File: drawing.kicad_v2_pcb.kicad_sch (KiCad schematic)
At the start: 39 parts, among them IC1 DW01A-G, J1 Micro USB Chargeport, J2 Prog headers, J3 128x32 I2C OLED, J4 TP4056, J5 MK-12C02, J6 Conn_01x02, Q1 FS8205, U1 HT7333-SOT89, U2 ESP-12E, U3 ATTINY85-20PU

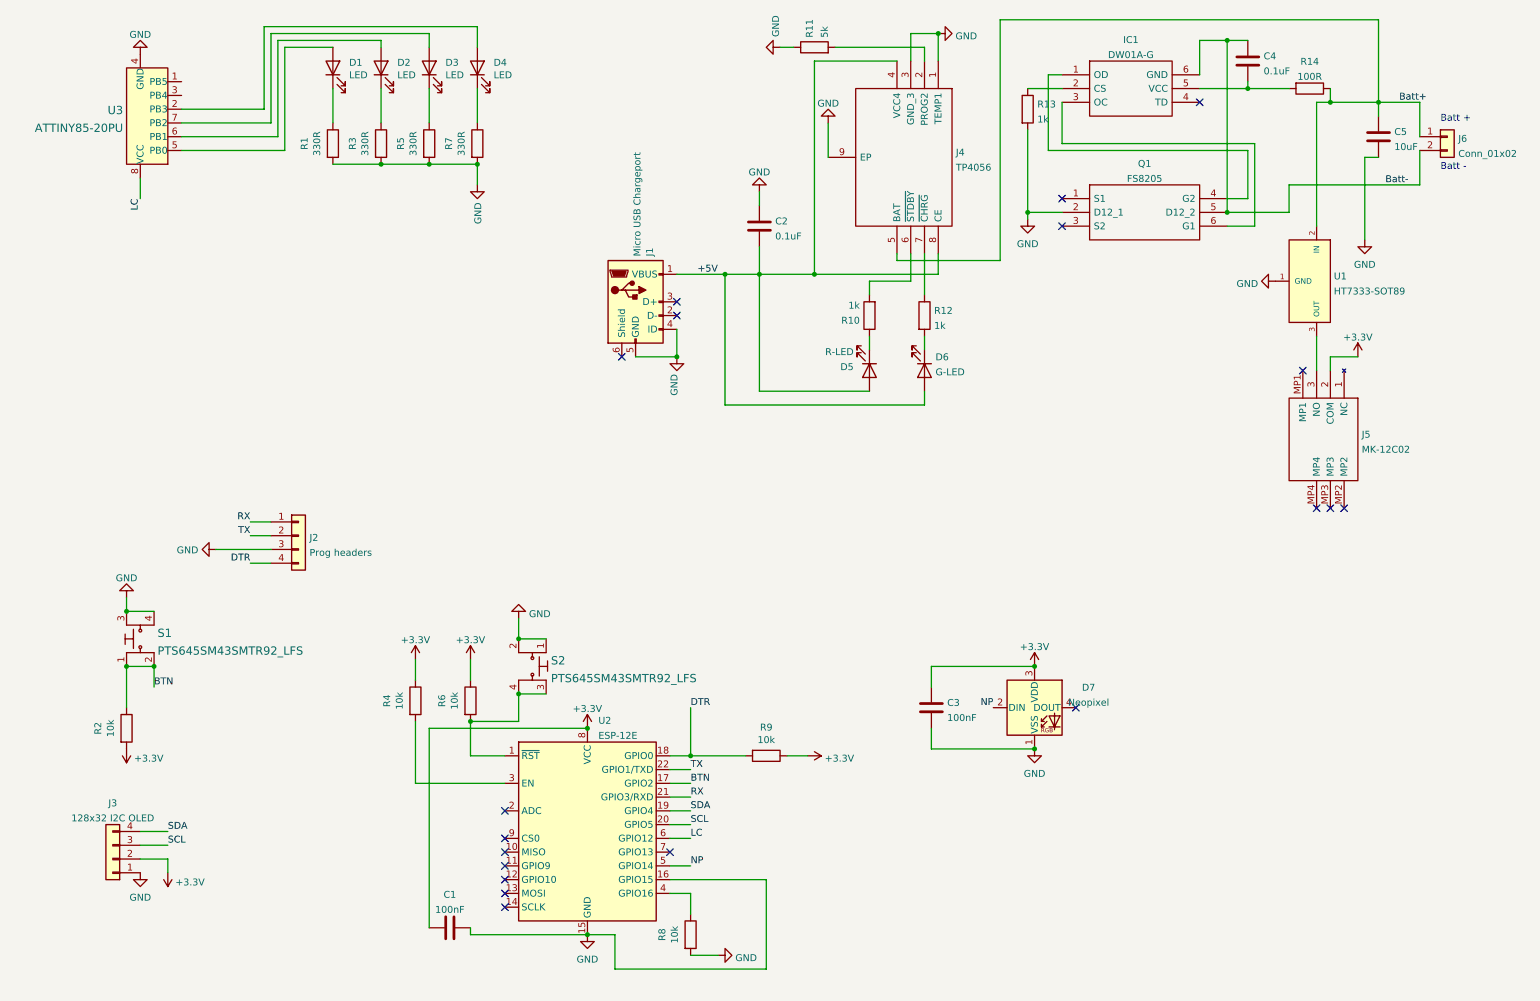
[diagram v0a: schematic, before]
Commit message: Fixed HT7333 and charging circuit
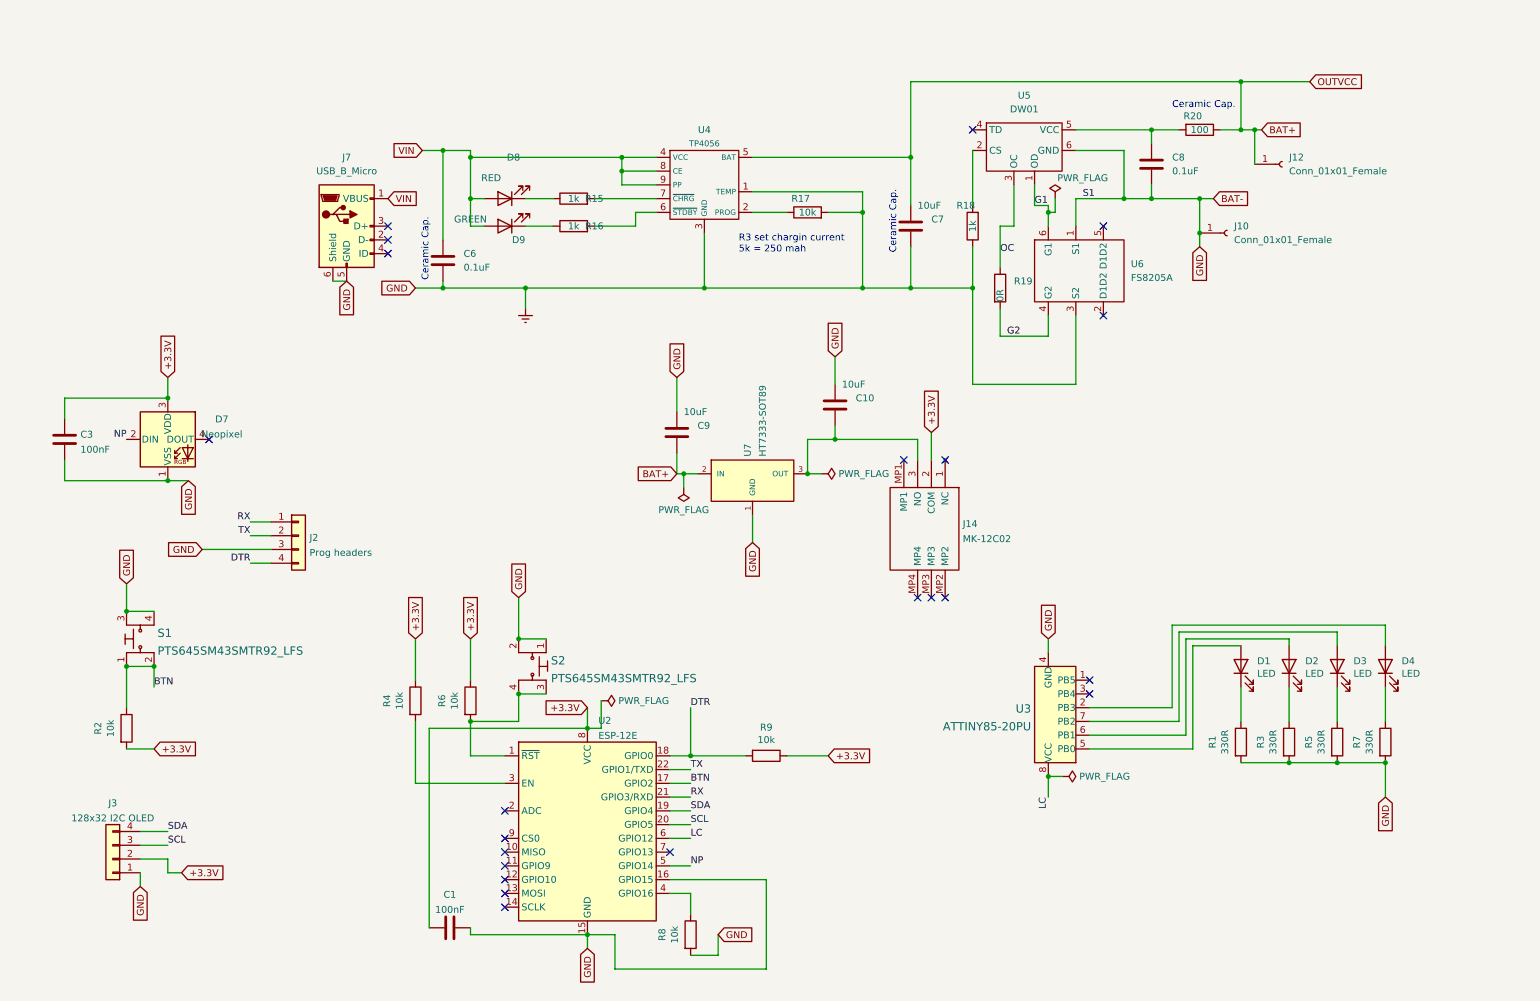
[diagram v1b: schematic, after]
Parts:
- removed C2, C4: 0.1uF, Capacitor_SMD:C_0805_2012Metric_Pad1.18x1.45mm_HandSolder, symbol Device:C
- removed C5: 10uF, Capacitor_SMD:C_0805_2012Metric_Pad1.18x1.45mm_HandSolder, symbol Device:C
- removed D5: R-LED, LED_SMD:LED_0805_2012Metric_Pad1.15x1.40mm_HandSolder, symbol Device:LED
- removed D6: G-LED, LED_SMD:LED_0805_2012Metric_Pad1.15x1.40mm_HandSolder, symbol Device:LED
- removed IC1: DW01A-G, user-footprints:SOT95P280X135-6N, symbol DW01A-G:DW01A-G
- removed J1: Micro USB Chargeport, digikey-footprints:USB_Micro_B_Female_10118194-0001LF, symbol Connector:USB_B_Micro
- removed J4: TP4056, Custom:SOIC127P600X175-9N, symbol TP4056:TP4056
- removed J5: MK-12C02, user-footprints:MK12C02, symbol MK-12C02:MK-12C02
- removed J6: Conn_01x02, Connector_JST:JST_EH_B2B-EH-A_1x02_P2.50mm_Vertical, symbol Connector_Generic:Conn_01x02
- removed Q1: FS8205, user-footprints:FS8205, symbol FS8205:FS8205
- removed R10, R12, R13: 1k, Resistor_SMD:R_0805_2012Metric_Pad1.20x1.40mm_HandSolder, symbol Device:R
- removed R11: 5k, Resistor_SMD:R_0805_2012Metric_Pad1.20x1.40mm_HandSolder, symbol Device:R
- removed R14: 100R, Resistor_SMD:R_0805_2012Metric_Pad1.20x1.40mm_HandSolder, symbol Device:R
- removed U1: HT7333-SOT89, Custom:Holtek-HT7333-SOT89-Level_A, symbol eec:HT7333-SOT89
- added C10, C7, C9: 10uF, Capacitor_SMD:C_0805_2012Metric_Pad1.18x1.45mm_HandSolder, symbol Device:C
- added C6, C8: 0.1uF, Capacitor_SMD:C_0805_2012Metric_Pad1.18x1.45mm_HandSolder, symbol Device:C
- added D8: RED, LED_SMD:LED_0805_2012Metric_Pad1.15x1.40mm_HandSolder, symbol Device:LED
- added D9: GREEN, LED_SMD:LED_0805_2012Metric_Pad1.15x1.40mm_HandSolder, symbol Device:LED
- added J10, J12: Conn_01x01_Female, user-footprints:solderpad, symbol Connector:Conn_01x01_Female
- added J14: MK-12C02, user-footprints:MK12C02, symbol MK-12C02:MK-12C02
- added J7: USB_B_Micro, digikey-footprints:USB_Micro_B_Female_10118194-0001LF, symbol Connector:USB_B_Micro
- added R15, R16, R18: 1k, Resistor_SMD:R_0603_1608Metric_Pad0.98x0.95mm_HandSolder, symbol Device:R
- added R17: 10k, Resistor_SMD:R_0805_2012Metric_Pad1.20x1.40mm_HandSolder, symbol Device:R
- added R19: 0R, Resistor_SMD:R_1206_3216Metric_Pad1.30x1.75mm_HandSolder, symbol Device:R
- added R20: 100, Resistor_SMD:R_0805_2012Metric_Pad1.20x1.40mm_HandSolder, symbol Device:R
- added U4: TP4056, Package_SO:SOIC-8-1EP_3.9x4.9mm_P1.27mm_EP2.29x3mm, symbol tp4056:TP4056
- added U5: DW01, Package_TO_SOT_SMD:SOT-23-6_Handsoldering, symbol dw01:DW01
- added U6: FS8205A, Package_TO_SOT_SMD:SOT-23-6_Handsoldering, symbol fs8205:FS8205A
- added U7: HT7333-SOT89, user-footprints:Holtek-HT7333-SOT89-Level_A, symbol eec:HT7333-SOT89
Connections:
- net +3V3 renamed +3.3V
- net +3.3V: now also J14.2 (COM)
- net GND renamed Earth
- net Earth: now also C10.1, C6.2, C7.2, C8.2, C9.1, J10.1 (Pin_1), J7.5 (GND), J7.6 (Shield), R17.2, R18.1, U4.1 (TEMP), U4.3 (GND), U5.6 (GND), U6.1 (S1), U6.3 (S2), U7.1 (GND)
- new net: C10.2, J14.3 (NO), U7.3 (OUT)
- new net: R18.2, U5.2 (CS)
- new net: D9.1 (K), R16.1
- new net: R17.1, U4.2 (PROG)
- new net: R16.2, U4.6 (~{STDBY})
- new net: R15.2, U4.7 (~{CHRG})
- new net: C8.1, R20.2, U5.5 (VCC)
- new net: D8.1 (K), R15.1
- new net BAT+: C7.1, C9.2, J12.1 (Pin_1), R20.1, U4.5 (BAT), U7.2 (IN)
- new net G1: U5.1 (OD), U6.6 (G1)
- new net G2: R19.2, U6.4 (G2)
- new net OC: R19.1, U5.3 (OC)
- new net VIN: C6.1, D8.2 (A), D9.2 (A), J7.1 (VBUS), U4.4 (VCC), U4.8 (CE), U4.9 (PP)
- no-connect marks 19 -> 22
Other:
- note added: "Ceramic Cap."
- note added: "R3 set chargin current 5k = 250 mah"
- note removed: "Batt +"
- note removed: "Batt -"
- moved on the sheet: C3, D1, D2, D3, D4, D7, R1, R3, R5, R7, U3

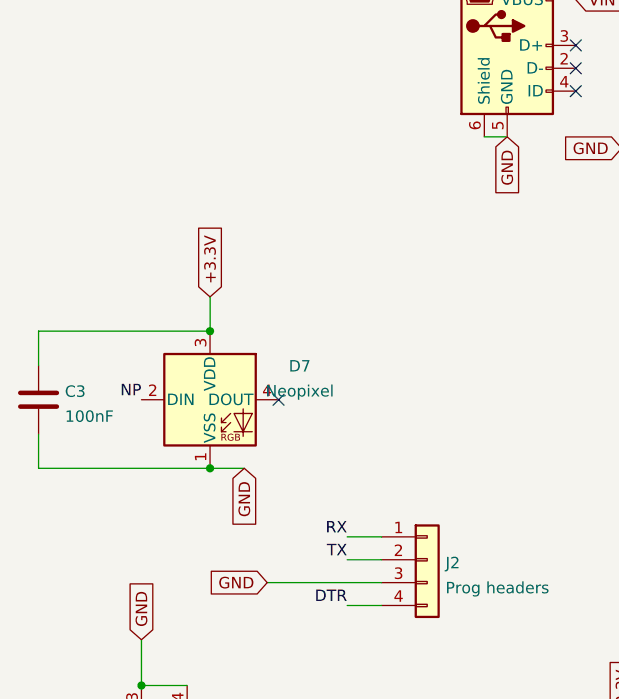
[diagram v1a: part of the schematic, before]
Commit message: Changed TH components to SMD
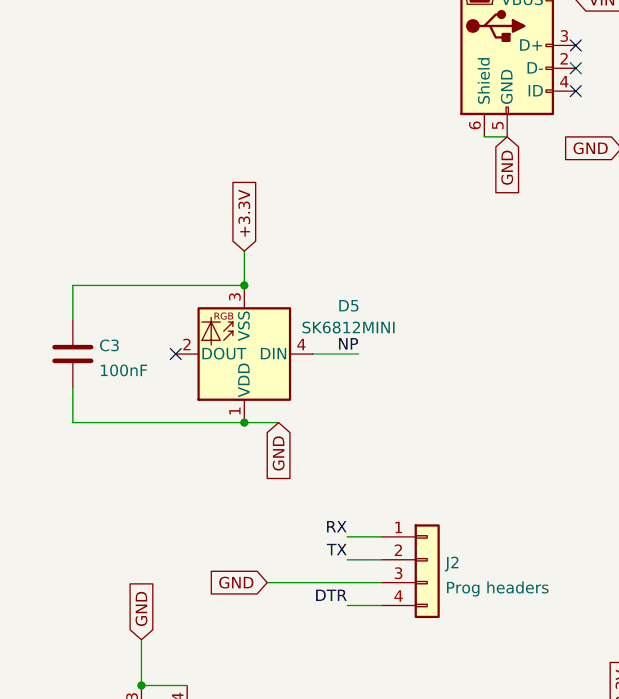
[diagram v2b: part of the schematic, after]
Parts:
- removed D7: Neopixel, user-footprints:LED_SK6812_PLCC4_5.0x5.0mm_P3.2mm_mirror, symbol LED:SK6812
- added D5: SK6812MINI, LED_SMD:LED_SK6812MINI_PLCC4_3.5x3.5mm_P1.75mm, symbol sk6812mini-e:SK6812MINI-E
- U3: footprint digikey-footprints:DIP-8_W7.62mm -> Package_DIP:SMDIP-8_W7.62mm
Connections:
- net +3.3V: now also D5.3 (VSS)
- net Earth: now also D5.1 (VDD)
- net NP: now also D5.4 (DIN)
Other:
- moved on the sheet: C3
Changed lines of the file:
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@@
   (junction (at 139.7 63.5) (diameter 0) (color 0 0 0 0)
   )
+  (junction (at 44.45 93.98) (diameter 0) (color 0 0 0 0)
+  )
   (junction (at 106.68 63.5) (diameter 0) (color 0 0 0 0)
   )
@@
   (junction (at 105.41 138.43) (diameter 0) (color 0 0 0 0)
   )
-  (junction (at 40.64 99.06) (diameter 0) (color 0 0 0 0)
+  (junction (at 44.45 78.74) (diameter 0) (color 0 0 0 0)
   )
   (junction (at 177.8 39.37) (diameter 0) (color 0 0 0 0)
@@
   )
   (junction (at 247.65 151.13) (diameter 0) (color 0 0 0 0)
-  )
-  (junction (at 40.64 83.82) (diameter 0) (color 0 0 0 0)
   )
   (junction (at 168.91 49.53) (diameter 0) (color 0 0 0 0)
@@
   (no_connect (at 213.36 52.07))
   (no_connect (at 184.15 95.25))
+  (no_connect (at 36.83 86.36))
   (no_connect (at 81.28 54.61))
   (no_connect (at 179.07 120.65))
@@
   (no_connect (at 102.87 172.72))
   (no_connect (at 102.87 175.26))
-  (no_connect (at 48.26 91.44))
   (no_connect (at 176.53 95.25))
   (no_connect (at 210.82 138.43))
@@
     (stroke (width 0) (type default))
   )
-  (wire (pts (xy 21.59 83.82) (xy 40.64 83.82))
+  (wire (pts (xy 25.4 78.74) (xy 44.45 78.74))
     (stroke (width 0) (type default))
   )
@@
     (stroke (width 0) (type default))
   )
-  (wire (pts (xy 21.59 87.63) (xy 21.59 83.82))
+  (wire (pts (xy 25.4 82.55) (xy 25.4 78.74))
     (stroke (width 0) (type default))
   )
@@
     (stroke (width 0) (type default))
   )
-  (wire (pts (xy 21.59 95.25) (xy 21.59 99.06))
+  (wire (pts (xy 25.4 90.17) (xy 25.4 93.98))
     (stroke (width 0) (type default))
   )
@@
     (stroke (width 0) (type default))
   )
-  (wire (pts (xy 21.59 99.06) (xy 40.64 99.06))
+  (wire (pts (xy 25.4 93.98) (xy 44.45 93.98))
     (stroke (width 0) (type default))
   )
@@
     (stroke (width 0) (type default))
   )
-  (wire (pts (xy 40.64 99.06) (xy 44.45 99.06))
-    (stroke (width 0) (type default))
-  )
   (wire (pts (xy 91.44 63.5) (xy 106.68 63.5))
     (stroke (width 0) (type default))
@@
     (stroke (width 0) (type default))
   )
+  (wire (pts (xy 52.07 86.36) (xy 57.15 86.36))
+    (stroke (width 0) (type default))
+  )
   (wire (pts (xy 238.76 151.13) (xy 247.65 151.13))
     (stroke (width 0) (type default))
@@
     (stroke (width 0) (type default))
   )
+  (wire (pts (xy 44.45 93.98) (xy 48.26 93.98))
+    (stroke (width 0) (type default))
+  )
   (wire (pts (xy 120.65 139.7) (xy 120.65 144.78))
     (stroke (width 0) (type default))
@@
     (stroke (width 0) (type default))
   )
-  (wire (pts (xy 40.64 80.01) (xy 40.64 83.82))
+  (wire (pts (xy 44.45 74.93) (xy 44.45 78.74))
     (stroke (width 0) (type default))
   )
@@
     (effects (font (size 1.27 1.27)) (justify left bottom))
   )
+  (label "NP" (at 57.15 86.36 180) (fields_autoplaced)
+    (effects (font (size 1.27 1.27)) (justify right bottom))
+  )
   (label "BTN" (at 38.1 137.16 0) (fields_autoplaced)
     (effects (font (size 1.27 1.27)) (justify left bottom))
@@
   (label "LC" (at 137.16 165.1 0) (fields_autoplaced)
     (effects (font (size 1.27 1.27)) (justify left bottom))
-  )
-  (label "NP" (at 33.02 91.44 180) (fields_autoplaced)
-    (effects (font (size 1.27 1.27)) (justify right bottom))
   )
   (label "DTR" (at 137.16 140.97 0) (fields_autoplaced)
@@
     )
   )
-  (global_label "+3.3V" (shape input) (at 40.64 80.01 90) (fields_autoplaced)
+  (global_label "+3.3V" (shape input) (at 44.45 74.93 90) (fields_autoplaced)
     (effects (font (size 1.27 1.27)) (justify left))
-    (property "Intersheetrefs" "${INTERSHEET_REFS}" (at 40.64 71.9942 90)
+    (property "Intersheetrefs" "${INTERSHEET_REFS}" (at 44.45 66.9142 90)
       (effects (font (size 1.27 1.27)) (justify left) hide)
     )
@@
     )
   )
-  (global_label "GND" (shape input) (at 44.45 99.06 270) (fields_autoplaced)
+  (global_label "GND" (shape input) (at 48.26 93.98 270) (fields_autoplaced)
     (effects (font (size 1.27 1.27)) (justify right))
-    (property "Intersheetrefs" "${INTERSHEET_REFS}" (at 44.45 105.2615 90)
+    (property "Intersheetrefs" "${INTERSHEET_REFS}" (at 48.26 100.1815 90)
       (effects (font (size 1.27 1.27)) (justify right) hide)
     )
@@
       (effects (font (size 1.524 1.524)) (justify left))
     )
-    (property "Footprint" "digikey-footprints:DIP-8_W7.62mm" (at 200.66 148.59 0)
+    (property "Footprint" "Package_DIP:SMDIP-8_W7.62mm" (at 200.66 148.59 0)
       (effects (font (size 1.524 1.524)) (justify left) hide)
     )
@@
     )
   )
+  (symbol (lib_id "sk6812mini-e:SK6812MINI-E") (at 44.45 86.36 180) (unit 1)
+    (in_bom yes) (on_board yes) (dnp no) (fields_autoplaced)
+    (property "Reference" "D5" (at 56.0577 81.0376 0)
+      (effects (font (size 1.27 1.27)))
+    )
+    (property "Value" "SK6812MINI" (at 56.0577 83.4618 0)
+      (effects (font (size 1.27 1.27)))
+    )
+    (property "Footprint" "LED_SMD:LED_SK6812MINI_PLCC4_3.5x3.5mm_P1.75mm" (at 43.18 78.74 0)
+      (effects (font (size 1.27 1.27)) (justify left top) hide)
+    )
+    (property "Datasheet" "https://cdn-shop.adafruit.com/product-files/2686/SK6812MINI_REV.01-1-2.pdf" (at 41.91 76.835 0)
+      (effects (font (size 1.27 1.27)) (justify left top) hide)
+    )
+    (pin "1")
+    (pin "2")
+    (pin "3")
+    (pin "4")
+    (instances
+      (project "drawing.kicad_v2_pcb"
+        (path "/746ba970-8279-4e7b-aed3-f28687777c21"
+          (reference "D5") (unit 1)
+        )
+      )
+    )
+  )
   (symbol (lib_id "Device:R") (at 151.13 149.86 270) (unit 1)
     (in_bom yes) (on_board yes) (dnp no)
@@
     )
   )
-  (symbol (lib_id "LED:SK6812") (at 40.64 91.44 0) (unit 1)
-    (in_bom yes) (on_board yes) (dnp no) (fields_autoplaced)
-    (property "Reference" "D7" (at 50.6133 87.7148 0)
-      (effects (font (size 1.27 1.27)))
-    )
-    (property "Value" "Neopixel" (at 50.6133 90.4899 0)
-      (effects (font (size 1.27 1.27)))
-    )
-    (property "Footprint" "user-footprints:LED_SK6812_PLCC4_5.0x5.0mm_P3.2mm_mirror" (at 41.91 99.06 0)
-      (effects (font (size 1.27 1.27)) (justify left top) hide)
-    )
-    (property "Datasheet" "https://cdn-shop.adafruit.com/product-files/1138/SK6812+LED+datasheet+.pdf" (at 43.18 100.965 0)
-      (effects (font (size 1.27 1.27)) (justify left top) hide)
-    )
-    (pin "1")
-    (pin "2")
-    (pin "3")
-    (pin "4")
-    (instances
-      (project "drawing.kicad_v2_pcb"
-        (path "/746ba970-8279-4e7b-aed3-f28687777c21"
-          (reference "D7") (unit 1)
-        )
-      )
-    )
-  )
   (symbol (lib_id "Device:LED") (at 102.87 46.99 180) (unit 1)
     (in_bom yes) (on_board yes) (dnp no)
@@
     )
   )
-  (symbol (lib_id "Device:C") (at 21.59 91.44 180) (unit 1)
+  (symbol (lib_id "Device:C") (at 25.4 86.36 180) (unit 1)
     (in_bom yes) (on_board yes) (dnp no) (fields_autoplaced)
-    (property "Reference" "C3" (at 24.511 90.5315 0)
+    (property "Reference" "C3" (at 28.321 85.4515 0)
       (effects (font (size 1.27 1.27)) (justify right))
     )
-    (property "Value" "100nF" (at 24.511 93.3066 0)
+    (property "Value" "100nF" (at 28.321 88.2266 0)
       (effects (font (size 1.27 1.27)) (justify right))
     )
-    (property "Footprint" "Capacitor_SMD:C_0805_2012Metric_Pad1.18x1.45mm_HandSolder" (at 20.6248 87.63 0)
-      (effects (font (size 1.27 1.27)) hide)
-    )
-    (property "Datasheet" "~" (at 21.59 91.44 0)
-      (effects (font (size 1.27 1.27)) hide)
-    )
+    (property "Footprint" "Capacitor_SMD:C_0805_2012Metric_Pad1.18x1.45mm_HandSolder" (at 24.4348 82.55 0)
+      (effects (font (size 1.27 1.27)) hide)
+    )
+    (property "Datasheet" "~" (at 25.4 86.36 0)
+      (effects (font (size 1.27 1.27)) hide)
+    )
